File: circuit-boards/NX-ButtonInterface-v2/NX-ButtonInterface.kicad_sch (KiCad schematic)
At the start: 2 parts, among them J1 NX CONTROL & UART, J2 NX BUTTON

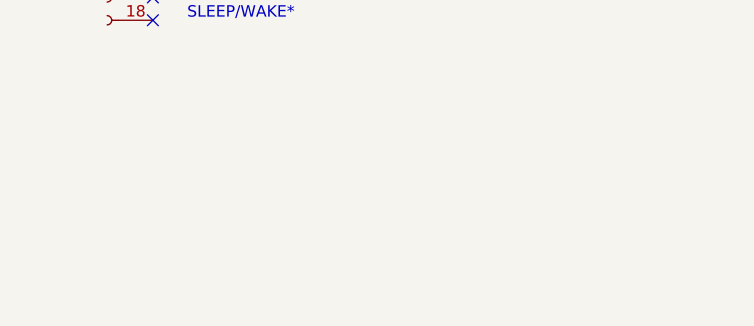
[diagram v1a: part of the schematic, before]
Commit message: adjust header to match nx-adapter
Signed-off-by: Scott Berman <sgberman1@gmail.com>
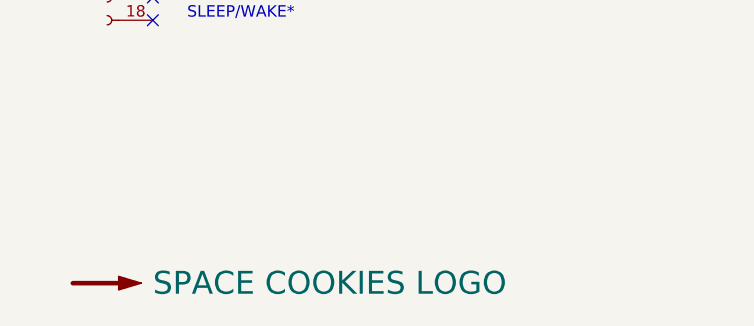
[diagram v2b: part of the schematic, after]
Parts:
- added LOGO1: SPACE COOKIES LOGO, NX-ButtonInterface:SPACE_COOKIES_LOGO_15mm, symbol Graphic:SYM_Arrow_Large
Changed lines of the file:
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@@
+		)
+	)
+	(symbol
+		(lib_id "Graphic:SYM_Arrow_Large")
+		(at 86.36 144.78 0)
+		(unit 1)
+		(exclude_from_sim no)
+		(in_bom no)
+		(on_board yes)
+		(dnp no)
+		(property "Reference" "LOGO1"
+			(at 86.36 142.494 0)
+			(effects
+				(font
+					(size 1.27 1.27)
+				)
+				(hide yes)
+			)
+		)
+		(property "Value" "SPACE COOKIES LOGO"
+			(at 91.44 144.78 0)
+			(effects
+				(font
+					(size 2.54 2.54)
+				)
+				(justify left)
+			)
+		)
+		(property "Footprint" "NX-ButtonInterface:SPACE_COOKIES_LOGO_15mm"
+			(at 86.36 144.78 0)
+			(effects
+				(font
+					(size 1.27 1.27)
+				)
+				(hide yes)
+			)
+		)
+		(property "Datasheet" ""
+			(at 86.36 144.78 0)
+			(effects
+				(font
+					(size 1.27 1.27)
+				)
+				(hide yes)
+			)
+		)
+		(property "Description" ""
+			(at 86.36 144.78 0)
+			(effects
+				(font
+					(size 1.27 1.27)
+				)
+				(hide yes)
+			)
+		)
+		(instances
+			(project "NX-ButtonInterface"
+				(path "/a7eb5823-c87f-41de-b6ed-af0ad18b6b3c"
+					(reference "LOGO1")
+					(unit 1)
+				)
+			)
 		)
 	)
